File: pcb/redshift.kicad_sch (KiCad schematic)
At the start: 75 parts, among them IC1 LPC5526JEV98, J1 G-Switch GT-USB-7010ASV, J2 C145962, J3 C2935905, J4 Conn_ARM_JTAG_SWD_10, SW1 SW_SP, SW2 SW_SP, SW3 SW_SP, SW4 PTS810, U1 PAW3399DM‐T4QU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

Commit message: Fixes #25
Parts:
- L1: footprint Resistor_SMD:R_0603_1608Metric -> Inductor_SMD:L_0805_2012Metric

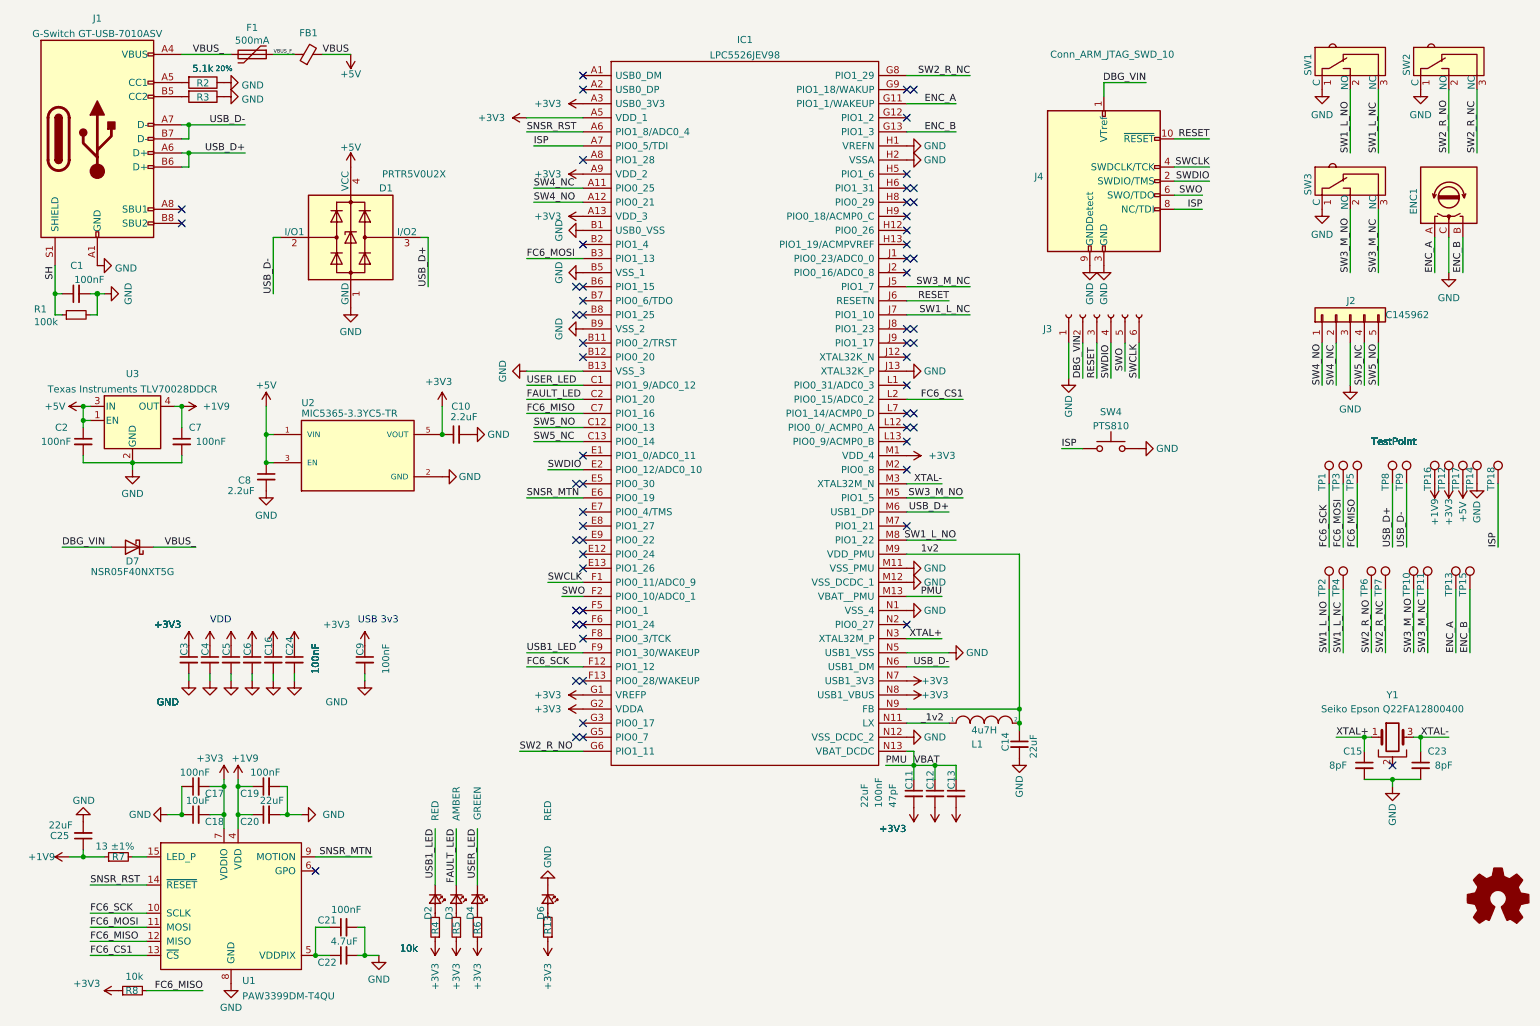
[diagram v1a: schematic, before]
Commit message: small fixes and updating board from schmatic
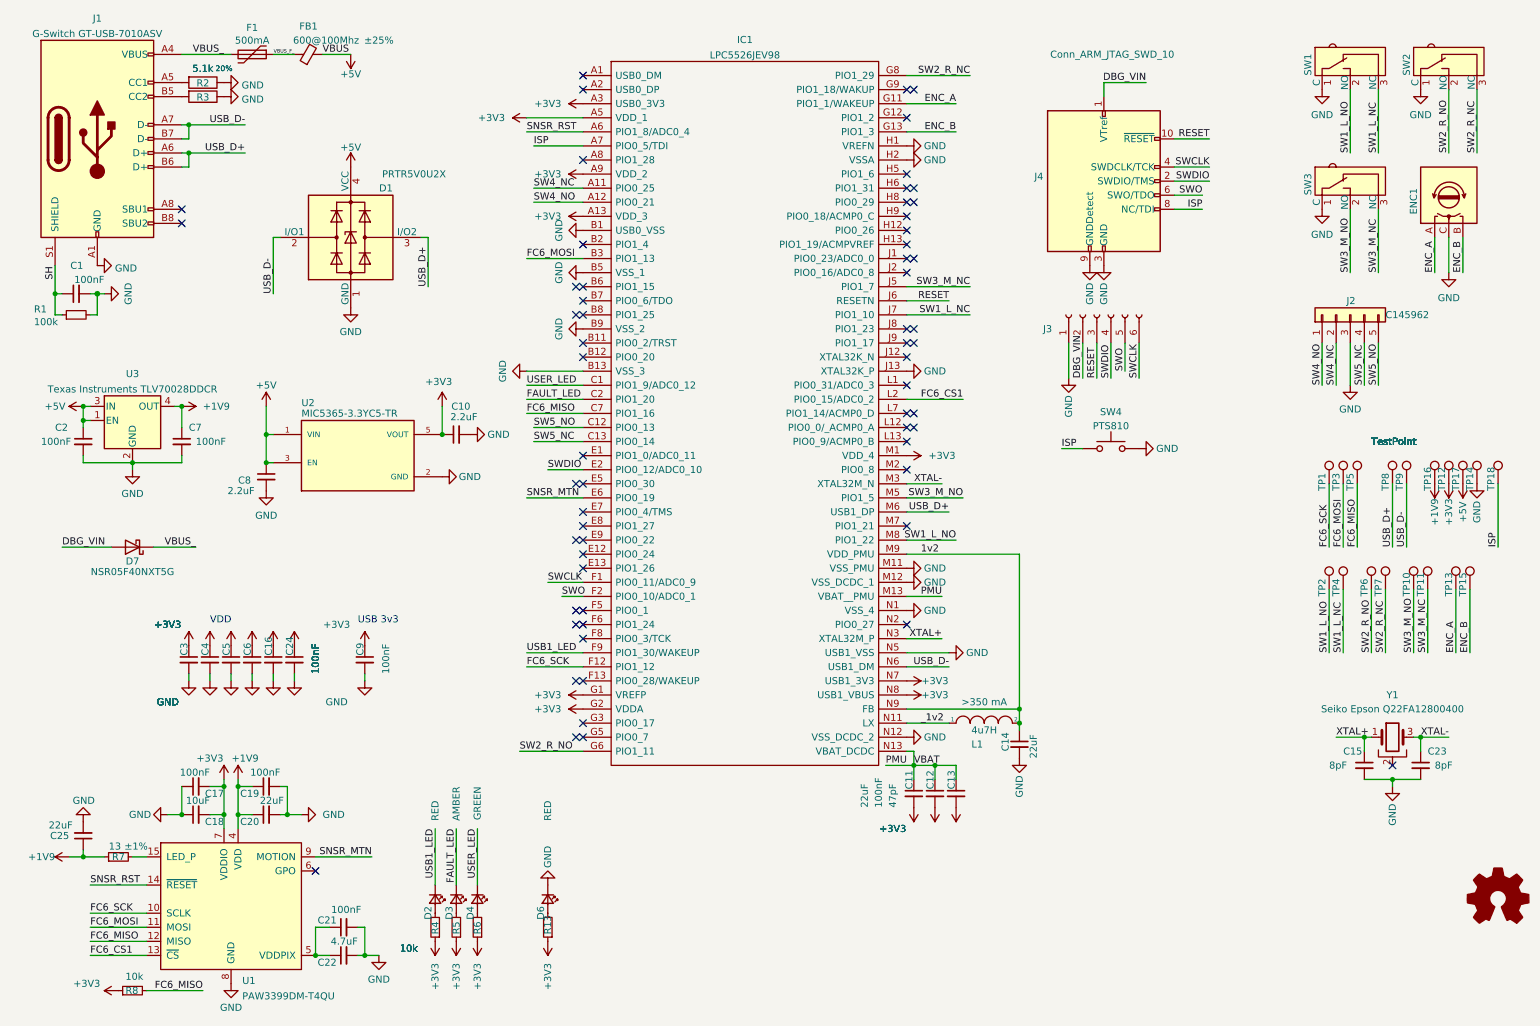
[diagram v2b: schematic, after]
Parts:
- FB1: value ~ -> 600@100Mhz; Tolerance (none) -> ±25%
- L1: Saturation Limit (none) -> >350 mA
- R7: value 13 ±1% -> 13; Tolerance (none) -> ±1%

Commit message: Add part numbers back based off of 64fe10091f3e64ca899d2226f0a24cf256eb9be7
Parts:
- C1, C12, C16, C17, C19, C2, C21, C24, C3, C4, C5, C6, C7, C9: LCSC (none) -> C1525
- C10, C8: LCSC (none) -> C12530
- C11, C14, C20, C25: LCSC (none) -> C59461
- C13: LCSC (none) -> C1567
- C15, C23: LCSC (none) -> C1578
- C18: LCSC (none) -> C15525
- C22: LCSC (none) -> C23733
- D1: LCSC (none) -> C12333
- D2, D6: LCSC (none) -> C965790
- D3, D4: LCSC (none) -> C401111
- D7: LCSC (none) -> C146713
- ENC1, J2, SW1, SW2, SW3, U1: now left out of the parts list
- F1: LCSC (none) -> C17168
- FB1: LCSC (none) -> C142082
- J1: LCSC (none) -> C2988369
- J4: LCSC (none) -> C2935458; now in the parts list
- L1: LCSC (none) -> C63166
- R1: LCSC (none) -> C25741
- R13, R4, R5, R6, R8: LCSC (none) -> C25744
- R2, R3: LCSC (none) -> C25905
- R7: LCSC (none) -> C368403
- SW4: LCSC (none) -> C231329
- U2: LCSC (none) -> C82942
- U3: LCSC (none) -> C507266
- Y1: LCSC (none) -> C255875

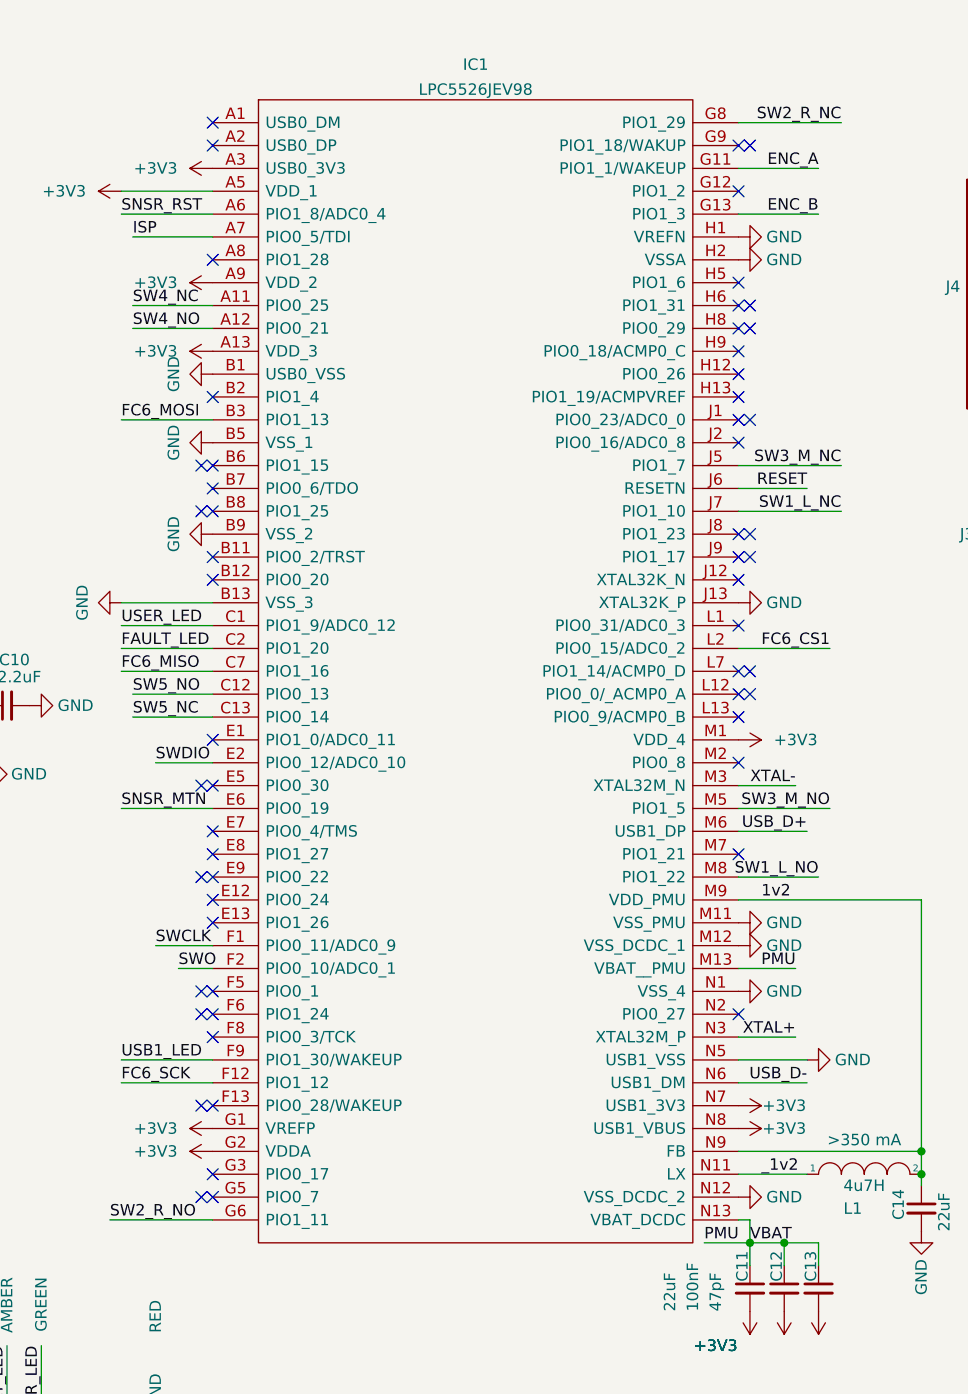
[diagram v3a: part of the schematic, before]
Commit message: Added Symbol for new chip to schematic
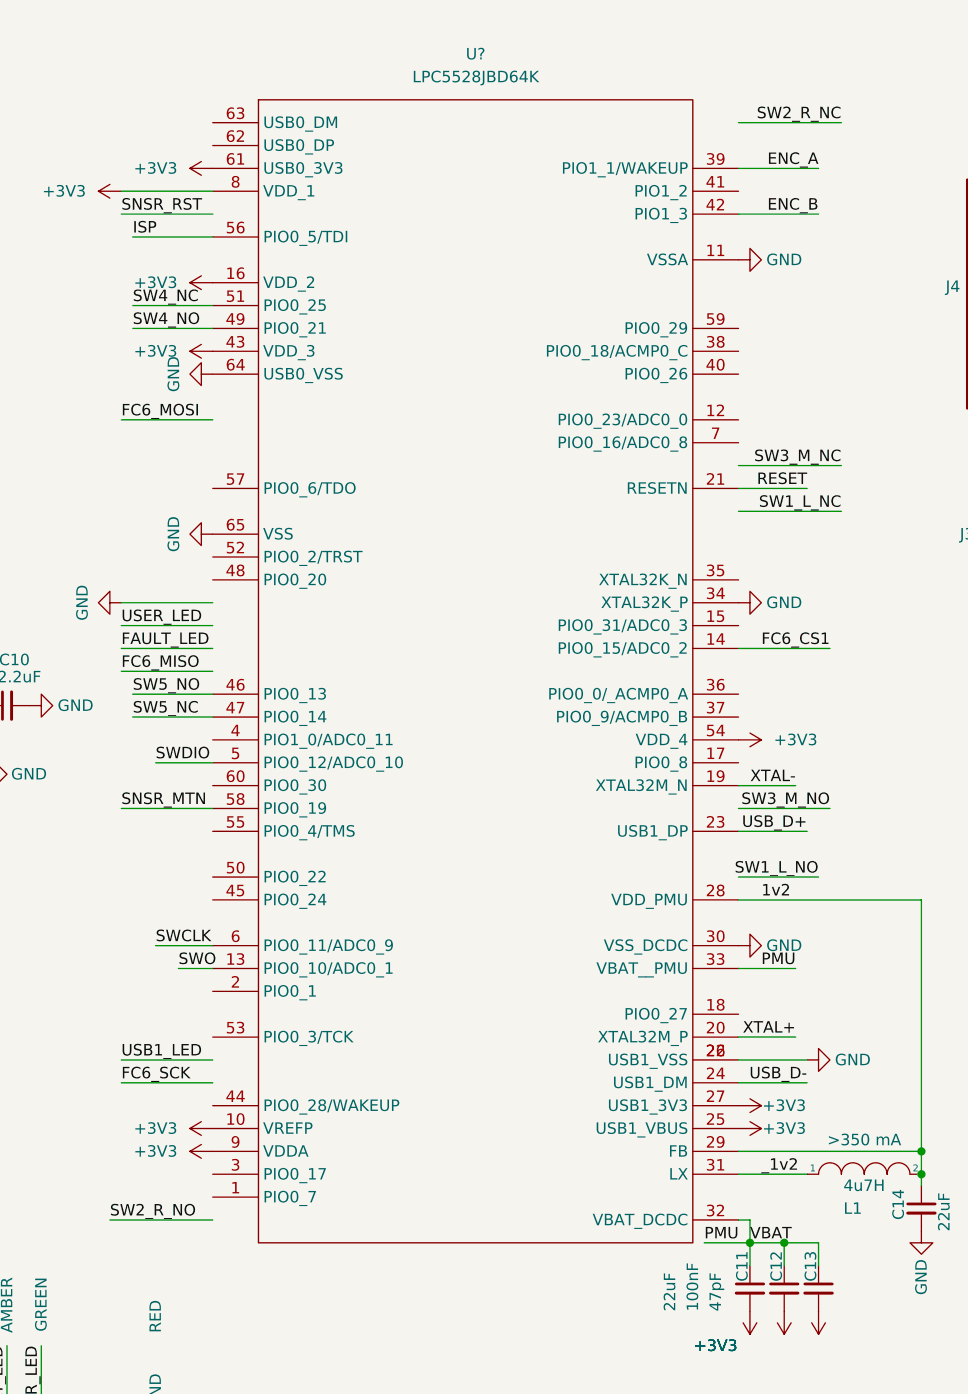
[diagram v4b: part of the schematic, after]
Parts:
- removed IC1: LPC5526JEV98, solokeys:BGA98C50P13X13_700X700X97N, symbol LPC5528JEV98K:LPC5528JEV98K
- added U?: LPC5528JBD64K, symbol LPC5528JBD64K:LPC5528JBD64K
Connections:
- net +3V3: now also U?.10 (VREFP), U?.16 (VDD_2), U?.25 (USB1_VBUS), U?.27 (USB1_3V3), U?.43 (VDD_3), U?.54 (VDD_4), U?.61 (USB0_3V3), U?.8 (VDD_1), U?.9 (VDDA)
- net 1v2: now also U?.28 (VDD_PMU), U?.29 (FB)
- net ENC_A: now also U?.39 (PIO1_1/WAKEUP)
- net ENC_B: now also U?.42 (PIO1_3)
- net FC6_CS1: now also U?.14 (PIO0_15/ADC0_2)
- net GND: now also U?.11 (VSSA), U?.22 (USB1_VSS), U?.26 (USB1_VSS), U?.30 (VSS_DCDC), U?.34 (XTAL32K_P), U?.64 (USB0_VSS), U?.65 (VSS)
- net ISP: now also U?.56 (PIO0_5/TDI)
- net PMU: now also U?.32 (VBAT_DCDC), U?.33 (VBAT__PMU)
- net RESET: now also U?.21 (RESETN)
- net SNSR_MTN: now also U?.58 (PIO0_19)
- net SW4_NC: now also U?.51 (PIO0_25)
- net SW4_NO: now also U?.49 (PIO0_21)
- net SW5_NC: now also U?.47 (PIO0_14)
- net SW5_NO: now also U?.46 (PIO0_13)
- net SWCLK: now also U?.6 (PIO0_11/ADC0_9)
- net SWDIO: now also U?.5 (PIO0_12/ADC0_10)
- net SWO: now also U?.13 (PIO0_10/ADC0_1)
- net USB_D+: now also U?.23 (USB1_DP)
- net USB_D-: now also U?.24 (USB1_DM)
- net XTAL+: now also U?.20 (XTAL32M_P)
- net XTAL-: now also U?.19 (XTAL32M_N)
- net _1v2: now also U?.31 (LX)
- no-connect marks 62 -> 4

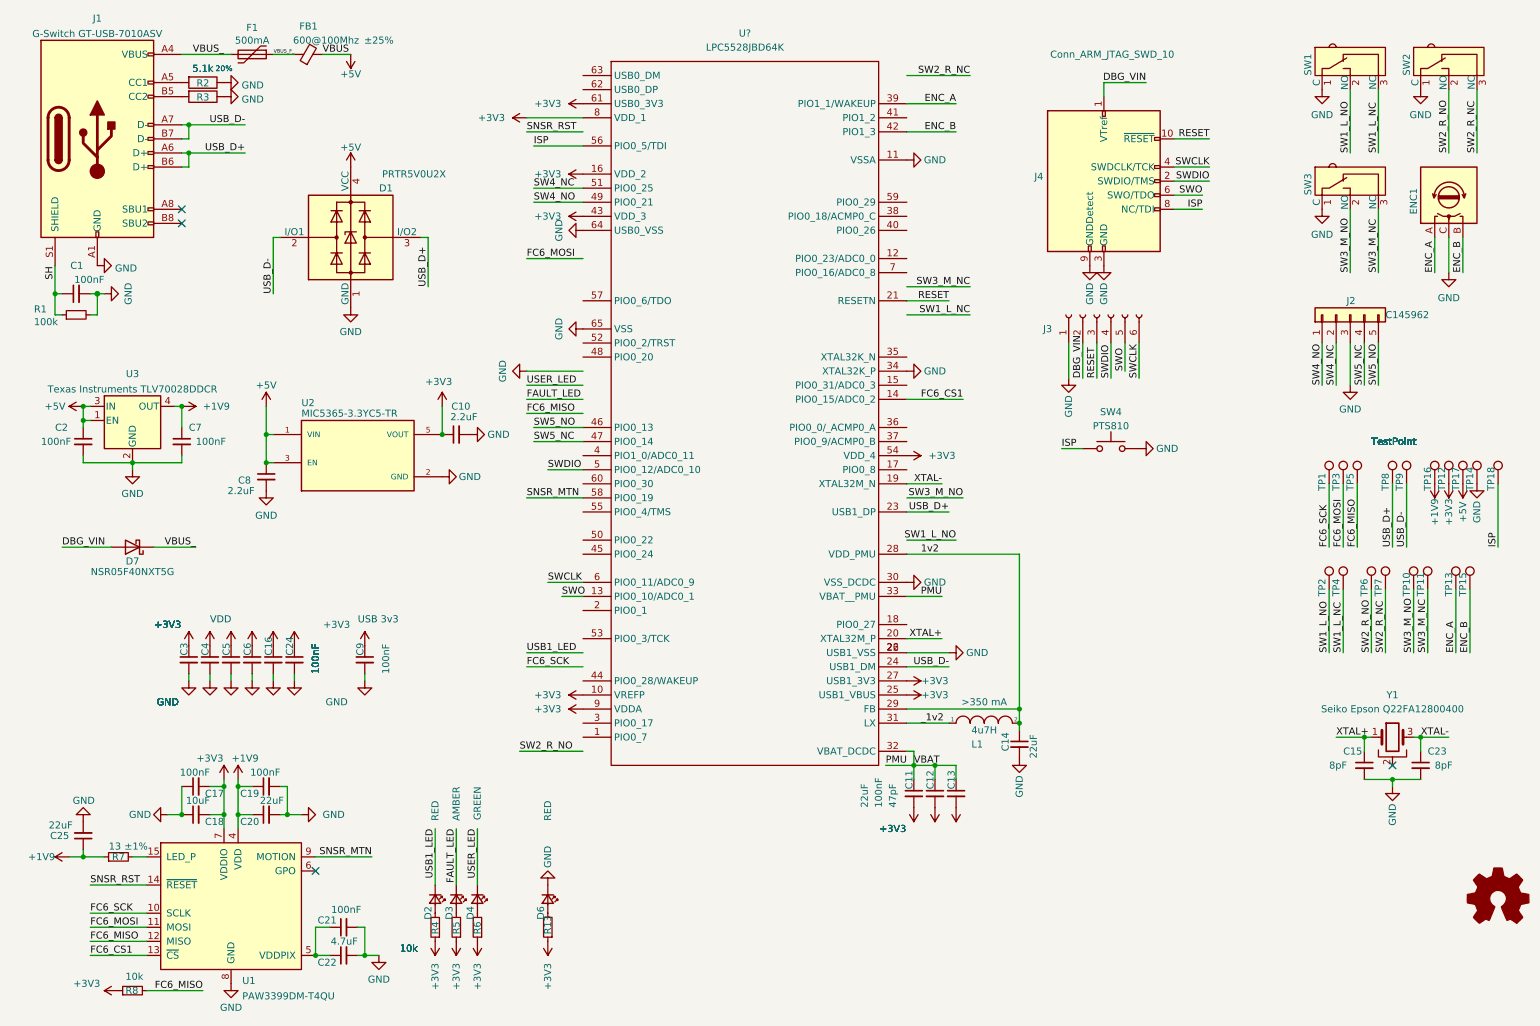
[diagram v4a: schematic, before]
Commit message: Reconnected paths that prev lead to deleted pins
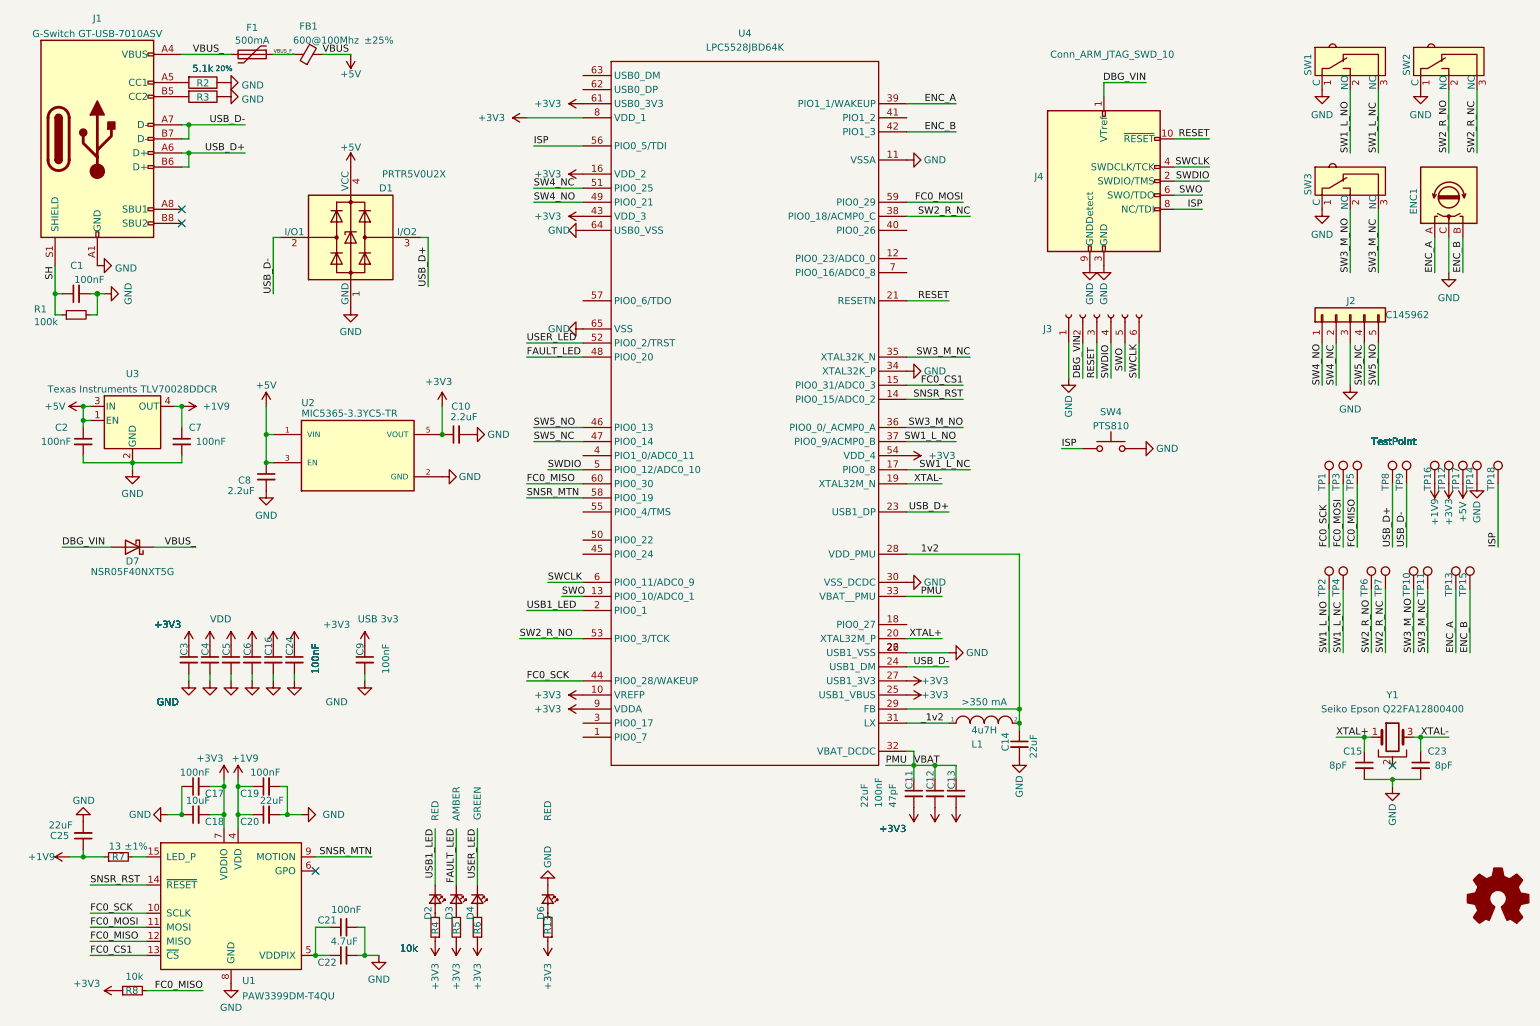
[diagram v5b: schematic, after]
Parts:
- gave numbers to parts that had none: 1
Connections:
- net FC6_MISO is gone; now on net FC0_MISO: R8.2, TP5.1, U1.12 (MISO)
- net FC6_MOSI is gone; now on net FC0_MOSI: TP3.1, U1.11 (MOSI)
- net FC6_SCK is gone; now on net FC0_SCK: TP1.1, U1.10 (SCLK)
- net FAULT_LED: now also U4.48 (PIO0_20)
- net SNSR_RST: now also U4.14 (PIO0_15/ADC0_2)
- net SW1_L_NC: now also U4.17 (PIO0_8)
- net SW1_L_NO: now also U4.37 (PIO0_9/ACMP0_B)
- net SW2_R_NC: now also U4.38 (PIO0_18/ACMP0_C)
- net SW2_R_NO: now also U4.53 (PIO0_3/TCK)
- net SW3_M_NC: now also U4.35 (XTAL32K_N)
- net SW3_M_NO: now also U4.36 (PIO0_0/_ACMP0_A)
- net USB1_LED: now also U4.2 (PIO0_1)
- net USER_LED: now also U4.52 (PIO0_2/TRST)
- net FC0_CS1: now reaches U4.15 (PIO0_31/ADC0_3)
- net FC0_CS1: now also U1.13 (~{CS})
- net FC0_SCK: now reaches U4.44 (PIO0_28/WAKEUP)
- net FC0_MOSI: now reaches U4.59 (PIO0_29)
- net FC0_MISO: now reaches U4.60 (PIO0_30)
- removed net FC6_CS1: U1.13 (~{CS}), U4.14 (PIO0_15/ADC0_2)
